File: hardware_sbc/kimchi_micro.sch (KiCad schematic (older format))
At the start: 35 parts, among them J1 Conn_01x06, J2 Conn_01x06, J3 Conn_01x04_MountingPin, J4 Conn_02x05_Odd_Even, SW1 SW_Push, SW2 SW_Push, SW3 SW_Push, U1 IMX8MM, U2 24C32, Y1 Crystal_GND24

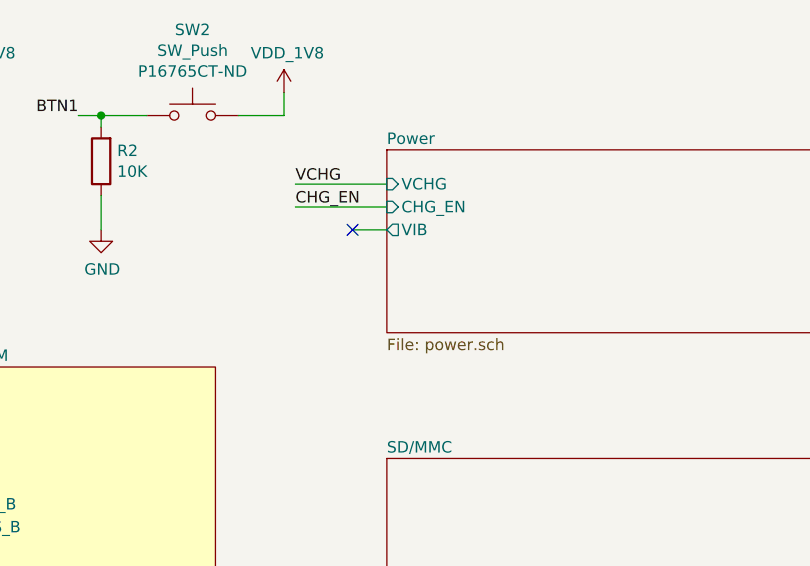
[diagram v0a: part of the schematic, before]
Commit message: Add battery monitor and protection circuit
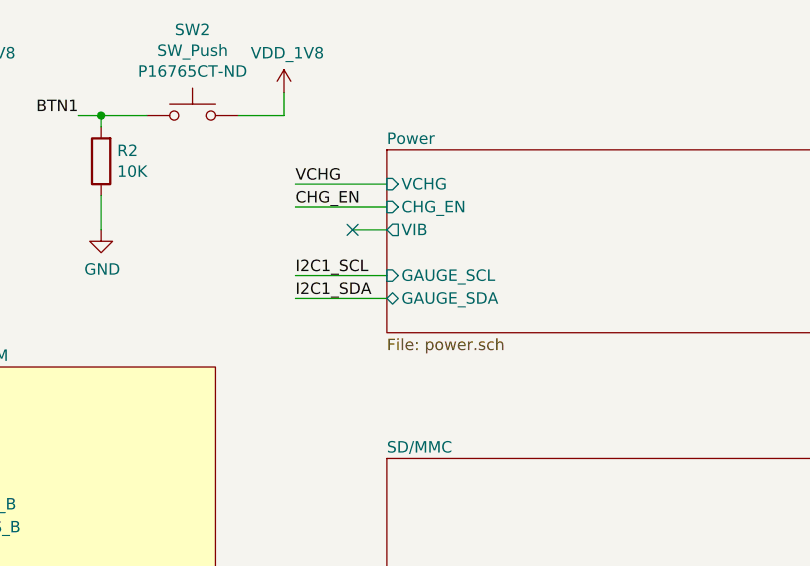
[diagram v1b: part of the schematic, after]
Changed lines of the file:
@@
 F3 "CHG_EN" I L 11000 1550 50
 F4 "VIB" O L 11000 1650 50
+F5 "GAUGE_SCL" I L 11000 1850 50
+F6 "GAUGE_SDA" B L 11000 1950 50
 $EndSheet
 Wire Wire Line
@@
 	1    0    0    -1
 $EndComp
+Text Label 10600 1850 0    50   ~ 0
+I2C1_SCL
+Wire Wire Line
+	10600 1850 11000 1850
+Text Label 10600 1950 0    50   ~ 0
+I2C1_SDA
+Wire Wire Line
+	10600 1950 11000 1950
 $EndSCHEMATC

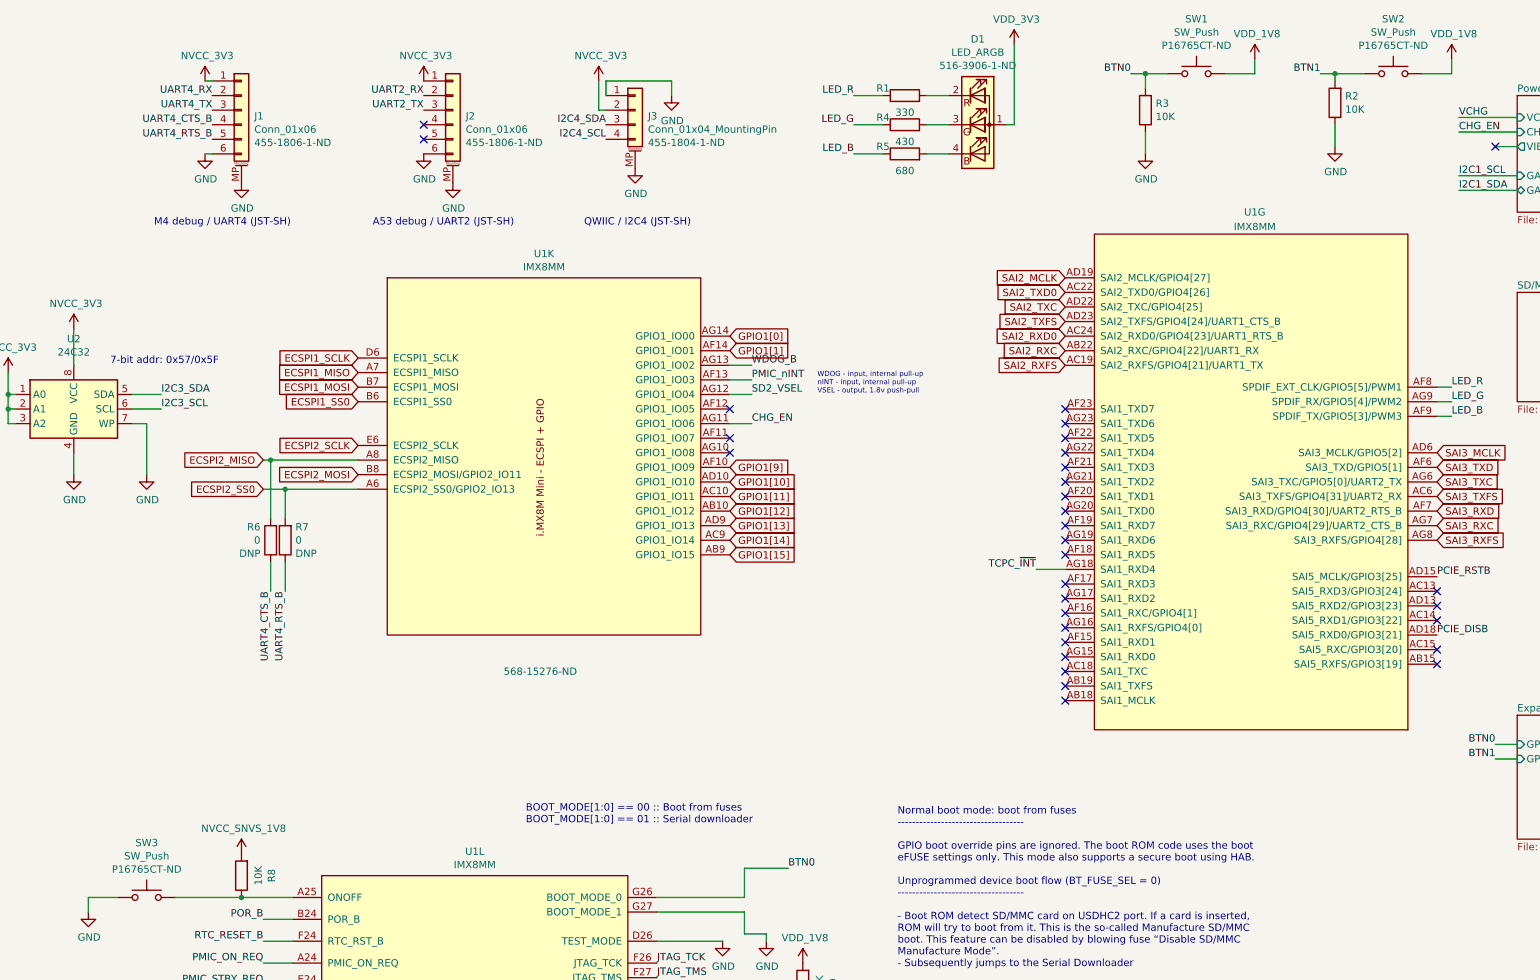
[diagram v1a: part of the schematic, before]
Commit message: BOM and misc fixes for production of 0.9 boards
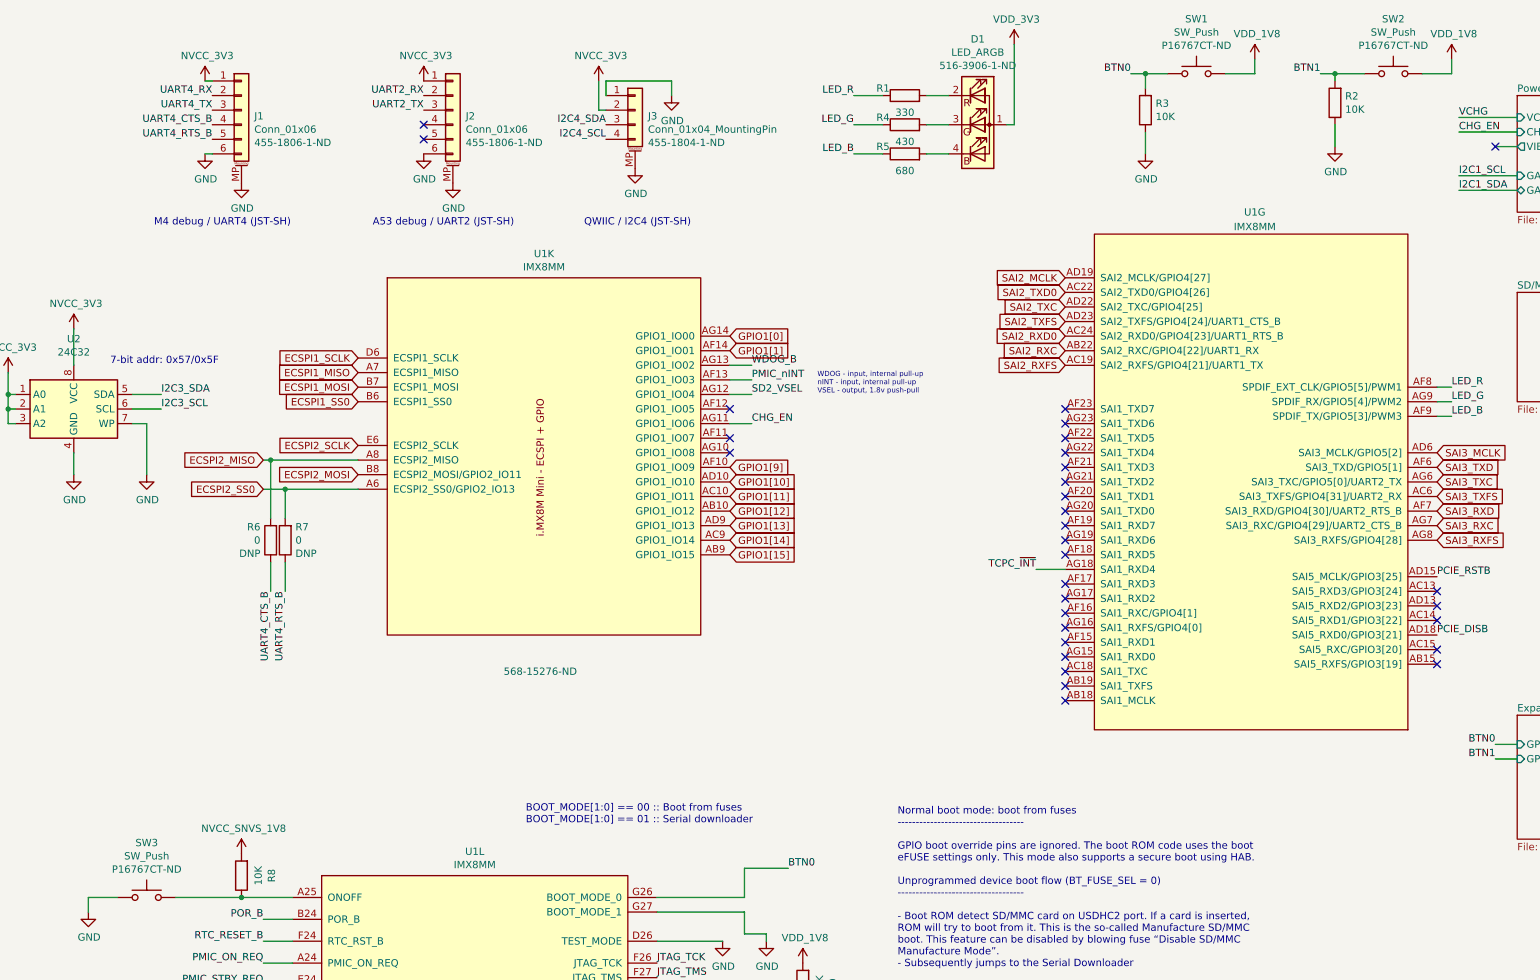
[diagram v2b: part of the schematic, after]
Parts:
- C1, C2: Mfgrpart (none) -> CGA1A2C0G1E120J030BA; Part CGA1A2C0G1E120J030BA -> (none)
- D1: Mfgrpart (none) -> ASMB-KTF0-0A306; Part ASMB-KTF0-0A306 -> (none)
- J1, J2: Mfgrpart (none) -> SM06B-SRSS-TB(LF)(SN); Part SM06B-SRSS-TB(LF)(SN) -> (none)
- J3: Mfgrpart (none) -> SM04B-SRSS-TB; Part SM04B-SRSS-TB -> (none)
- R1: Mfgrpart (none) -> RC0201JR-07330RL; Part RC0201JR-07330RL -> (none)
- R10, R2, R3, R8, R9: Mfgrpart (none) -> ERJ-1GNJ103C; Part ERJ-1GNJ103C -> (none)
- R11: Mfgrpart (none) -> RC0201JR-07100KL; Part RC0201JR-07100KL -> (none)
- R12, R13, R14, R15, R17, R18, R19, R20: Mfgrpart (none) -> RC0201JR-074K7L; Part RC0201JR-074K7L -> (none)
- R16: Mfgrpart (none) -> RC0201FR-07510KL; Part RC0201FR-07510KL -> (none)
- R4: Mfgrpart (none) -> RC0201JR-07430RL; Part RC0201JR-07430RL -> (none)
- R5: Mfgrpart (none) -> RC0201JR-07680RL; Part RC0201JR-07680RL -> (none)
- SW1, SW2, SW3: Mfgrpart (none) -> EVQ-P7J01P; Part EVQ-P7C01P -> (none); Vendorpart P16765CT-ND -> P16767CT-ND
- U1: Mfgrpart (none) -> MIMX8MM6CVTKZAA; Part MIMX8MM6CVTKZAA -> (none)
- U2: Mfgrpart (none) -> M24C32-FMC6TG; Part M24C32-FMC6TG -> (none)
- Y1: Mfgrpart (none) -> XRCGB24M000F0L00R0; Part XRCGB24M000F0L00R0 -> (none)

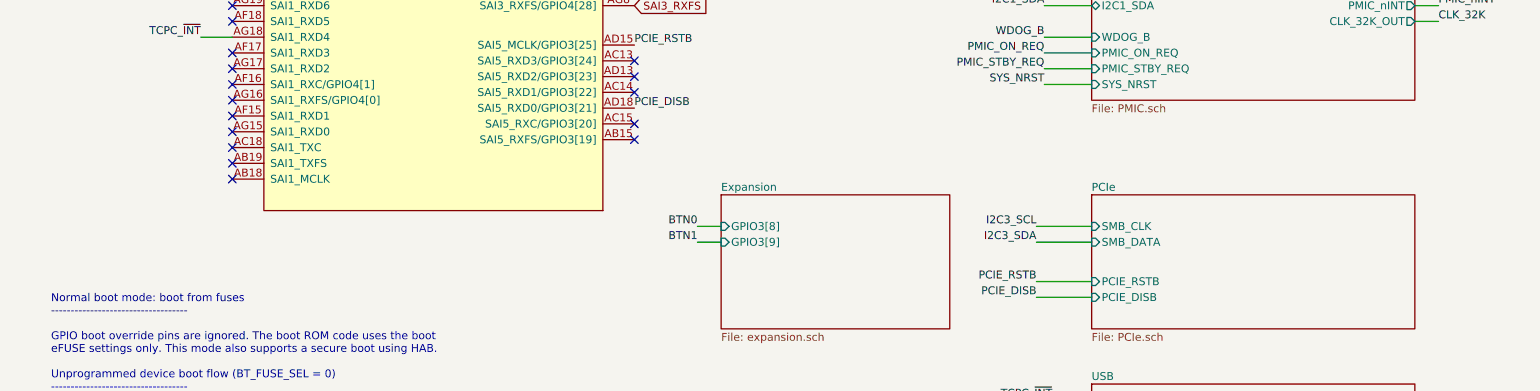
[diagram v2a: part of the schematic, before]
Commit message: Add load switch and separate power for VDD_PCIE_3V3
Fixes #3
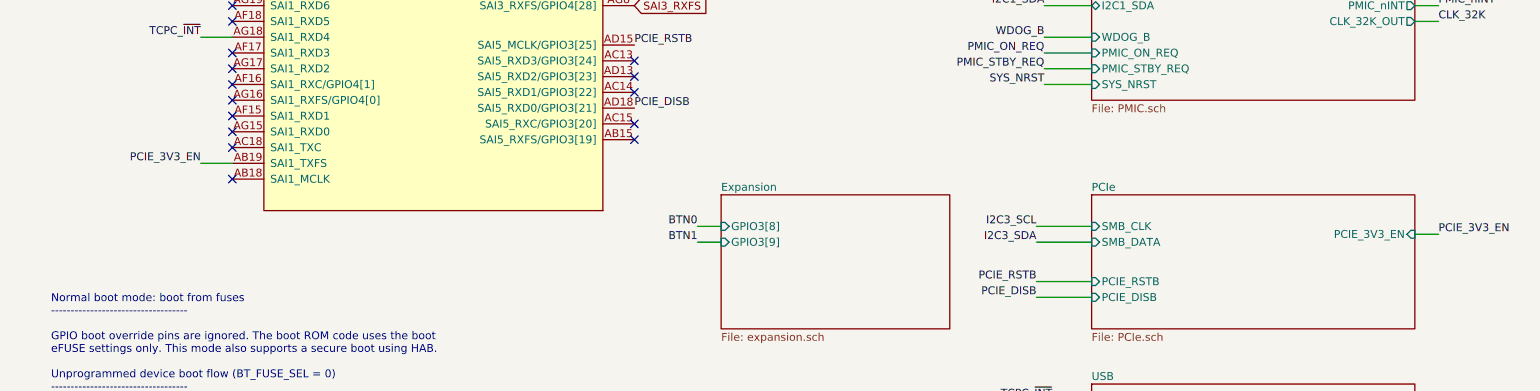
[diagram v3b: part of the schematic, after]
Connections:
- net PCIE_3V3_EN: now reaches U1.AB19 (SAI1_TXFS)
- no-connect marks 36 -> 35
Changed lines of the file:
@@
 F4 "PCIE_RSTB" I L 13350 6100 50
 F5 "PCIE_DISB" I L 13350 6200 50
+F6 "PCIE_3V3_EN" I R 15400 5800 50
 $EndSheet
 $Sheet
@@
 NoConn ~ 7900 4950
 NoConn ~ 7900 5050
-NoConn ~ 7900 5150
 NoConn ~ 7900 5250
-NoConn ~ 7900 5350
 NoConn ~ 7900 5450
 NoConn ~ 10450 4700
@@
 Wire Wire Line
 	10600 1950 11000 1950
+Text Label 15550 5800 0    50   ~ 0
+PCIE_3V3_EN
+Wire Wire Line
+	15550 5800 15400 5800
+Text Label 7700 5350 2    50   ~ 0
+PCIE_3V3_EN
+NoConn ~ 7900 5150
+Wire Wire Line
+	7700 5350 7900 5350
 $EndSCHEMATC

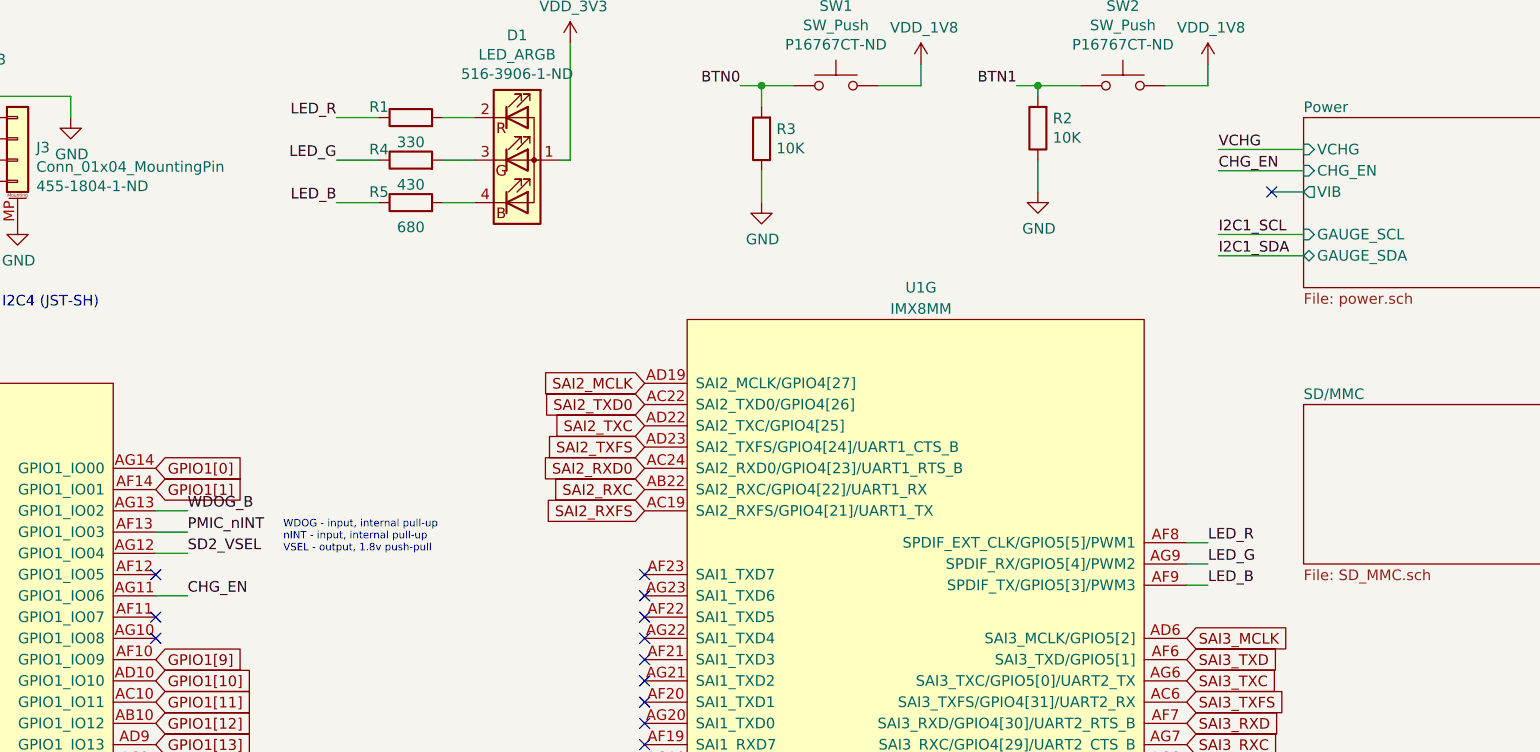
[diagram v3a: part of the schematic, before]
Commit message: Enable charging by default, remove processor control
Having the charge enable hooked up to the processor was problematic
when the pin is not configured. There's not a great case for needing
to have the processor enable/disable charging, so just leave it
enabled.
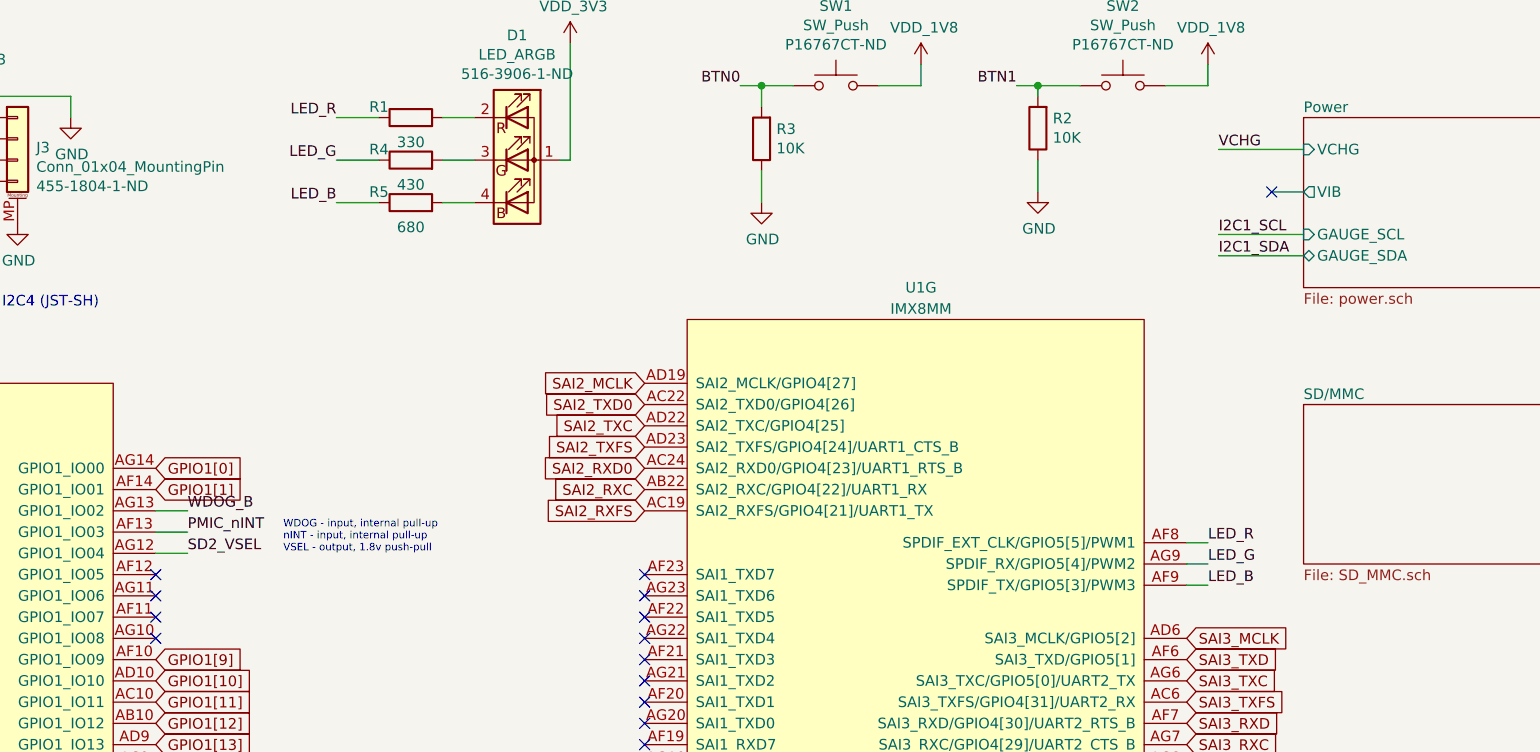
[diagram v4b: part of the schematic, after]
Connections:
- net CHG_EN: no longer names the net of U1.AG11 (GPIO1_IO06)
- no-connect marks 35 -> 36
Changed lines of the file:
@@
 F1 "power.sch" 50
 F2 "VCHG" I L 11000 1450 50
-F3 "CHG_EN" I L 11000 1550 50
-F4 "VIB" O L 11000 1650 50
-F5 "GAUGE_SCL" I L 11000 1850 50
-F6 "GAUGE_SDA" B L 11000 1950 50
+F3 "VIB" O L 11000 1650 50
+F4 "GAUGE_SCL" I L 11000 1850 50
+F5 "GAUGE_SDA" B L 11000 1950 50
 $EndSheet
 Wire Wire Line
@@
 Wire Wire Line
 	7700 4550 7900 4550
-Text Label 10600 1550 0    50   ~ 0
-CHG_EN
-Wire Wire Line
-	10600 1550 11000 1550
-Text Label 5750 3550 0    50   ~ 0
-CHG_EN
-Wire Wire Line
-	5750 3550 5600 3550
 $Comp
 L Connector_Generic_MountingPin:Conn_01x06_MountingPin J2
@@
 Wire Wire Line
 	7700 5350 7900 5350
+NoConn ~ 5600 3550
 $EndSCHEMATC
